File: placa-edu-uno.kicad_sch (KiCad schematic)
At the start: 7 parts, among them J1 Conn_02x20_Odd_Even_MountingP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, J2 Screw_Terminal_01x02, J3 Screw_Terminal_01x02, J4 Screw_Terminal_01x02, J5 Screw_Terminal_01x02, J6 Conn_02x13_Odd_Even

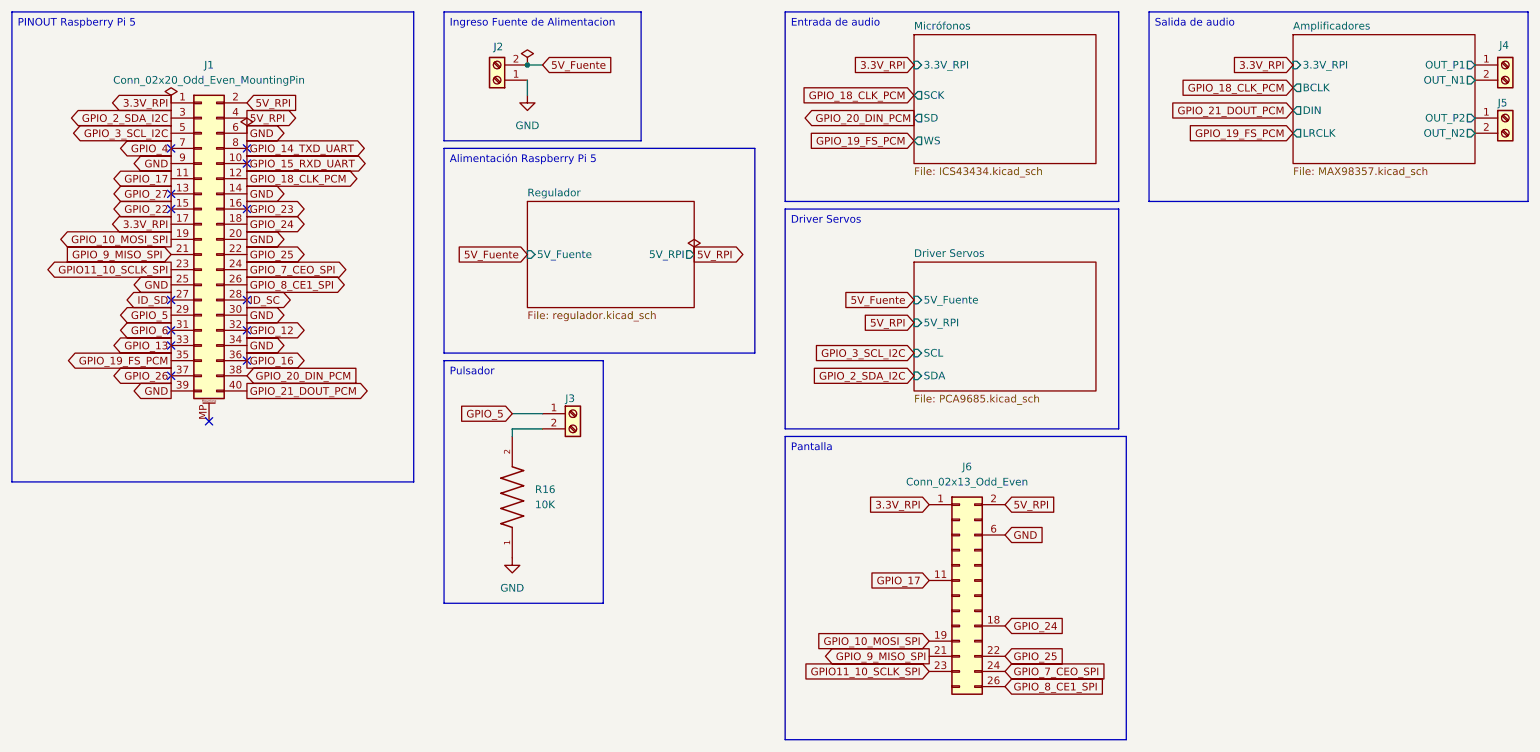
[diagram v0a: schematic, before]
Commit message: Se arranca un nuevo diseno. Se saco el regulador y 4 servos. Hay que reajustar el diseno del PCB.
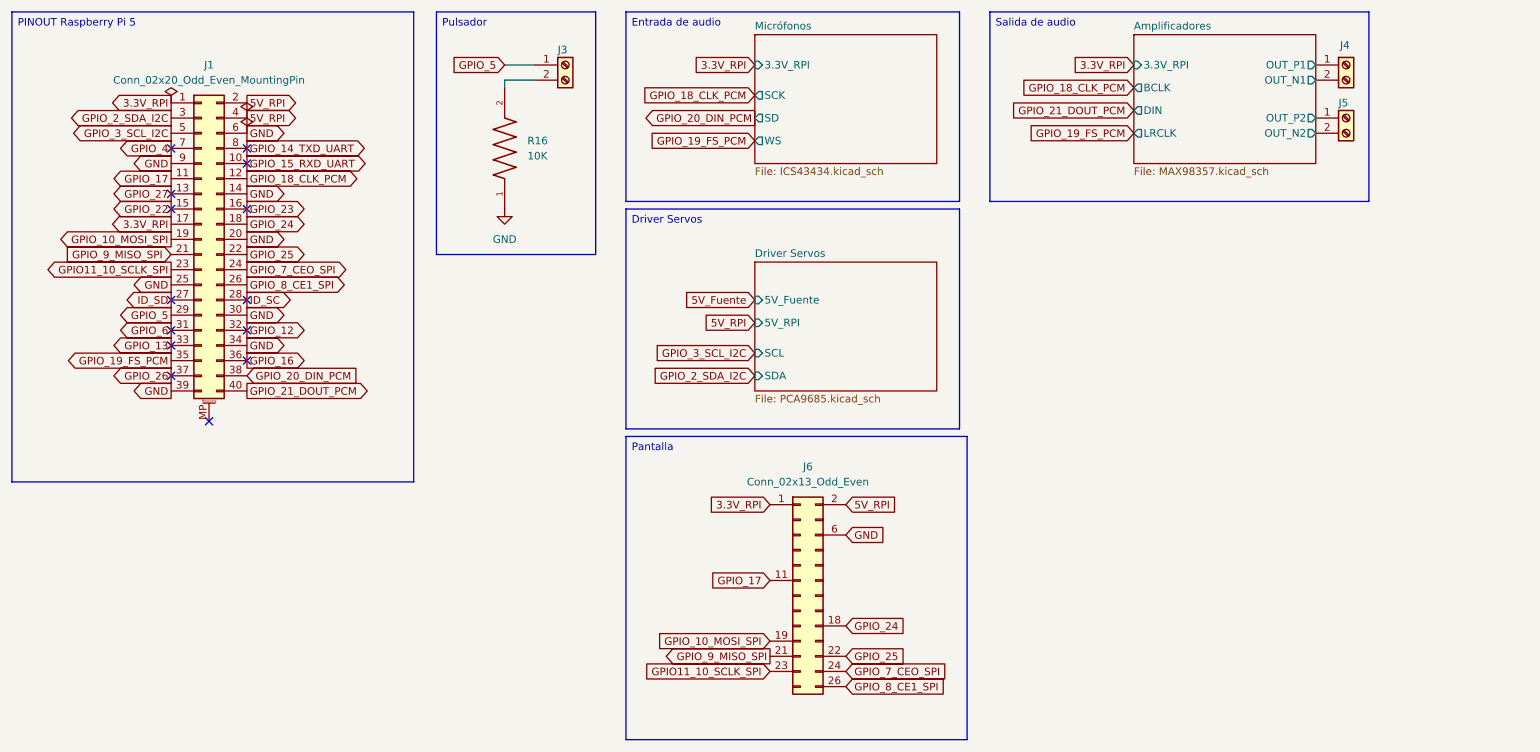
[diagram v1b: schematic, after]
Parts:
- removed J2: Screw_Terminal_01x02, 691253700002:691253700002, symbol Connector:Screw_Terminal_01x02
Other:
- removed sheet Regulador
- moved on the sheet: J3, J4, J5, J6, R16

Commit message: Se borro todo y se arranco de nuevo. Placa circular.
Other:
- sheet Driver Servos ports: added none; removed 5V_Fuente
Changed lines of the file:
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@@
 	(global_label "5V_RPI"
 		(shape input)
-		(at 147.32 80.01 180)
-		(fields_autoplaced yes)
-		(effects
-			(font
-				(size 1.27 1.27)
-			)
-			(justify right)
-		)
-		(property "Intersheetrefs" "${INTERSHEET_REFS}"
-			(at 137.9243 80.01 0)
+		(at 147.32 76.2 180)
+		(fields_autoplaced yes)
+		(effects
+			(font
+				(size 1.27 1.27)
+			)
+			(justify right)
+		)
+		(property "Intersheetrefs" "${INTERSHEET_REFS}"
+			(at 137.9243 76.2 0)
 			(effects
 				(font
@@
 	(global_label "GPIO_2_SDA_I2C"
 		(shape input)
-		(at 147.32 88.9 180)
-		(fields_autoplaced yes)
-		(effects
-			(font
-				(size 1.27 1.27)
-			)
-			(justify right)
-		)
-		(property "Intersheetrefs" "${INTERSHEET_REFS}"
-			(at 129.0948 88.9 0)
+		(at 147.32 85.09 180)
+		(fields_autoplaced yes)
+		(effects
+			(font
+				(size 1.27 1.27)
+			)
+			(justify right)
+		)
+		(property "Intersheetrefs" "${INTERSHEET_REFS}"
+			(at 129.0948 85.09 0)
 			(effects
 				(font
@@
 	(global_label "GPIO_3_SCL_I2C"
 		(shape input)
-		(at 147.32 85.09 180)
-		(fields_autoplaced yes)
-		(effects
-			(font
-				(size 1.27 1.27)
-			)
-			(justify right)
-		)
-		(property "Intersheetrefs" "${INTERSHEET_REFS}"
-			(at 129.1553 85.09 0)
+		(at 147.32 81.28 180)
+		(fields_autoplaced yes)
+		(effects
+			(font
+				(size 1.27 1.27)
+			)
+			(justify right)
+		)
+		(property "Intersheetrefs" "${INTERSHEET_REFS}"
+			(at 129.1553 81.28 0)
 			(effects
 				(font
@@
 				)
 				(justify left)
-				(hide yes)
-			)
-		)
-	)
-	(global_label "5V_Fuente"
-		(shape input)
-		(at 147.32 76.2 180)
-		(fields_autoplaced yes)
-		(effects
-			(font
-				(size 1.27 1.27)
-			)
-			(justify right)
-		)
-		(property "Intersheetrefs" "${INTERSHEET_REFS}"
-			(at 134.7796 76.2 0)
-			(effects
-				(font
-					(size 1.27 1.27)
-				)
-				(justify right)
 				(hide yes)
 			)
@@
 			)
 		)
-		(pin "5V_Fuente" input
+		(pin "5V_RPI" input
 			(at 147.32 76.2 180)
 			(effects
@@
 			)
 		)
-		(pin "5V_RPI" input
-			(at 147.32 80.01 180)
-			(effects
-				(font
-					(size 1.27 1.27)
-				)
-				(justify left)
-			)
-		)
 		(pin "SCL" input
+			(at 147.32 81.28 180)
+			(effects
+				(font
+					(size 1.27 1.27)
+				)
+				(justify left)
+			)
+		)
+		(pin "SDA" input
 			(at 147.32 85.09 180)
 			(effects
 				(font
-					(size 1.27 1.27)
-				)
-				(justify left)
-			)
-		)
-		(pin "SDA" input
-			(at 147.32 88.9 180)
-			(effects
-				(font
